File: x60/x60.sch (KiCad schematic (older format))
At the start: 154 parts, among them SW1 SW_Push, U1 ATmega32U4-AU, Y1 16mhz

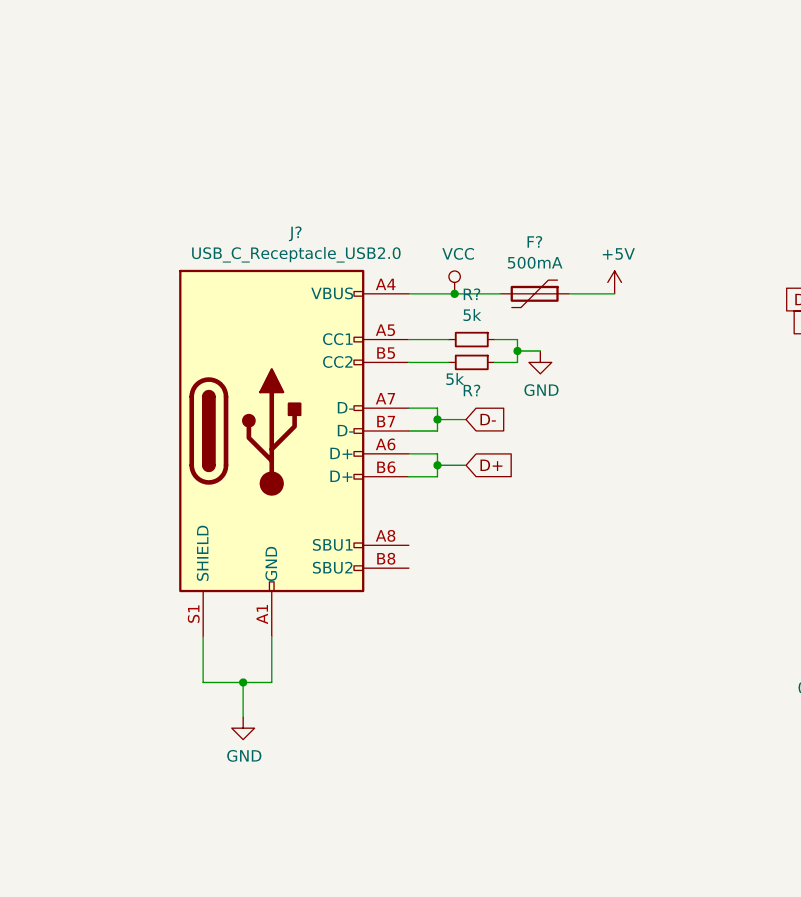
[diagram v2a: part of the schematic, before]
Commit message: redid usbc integration
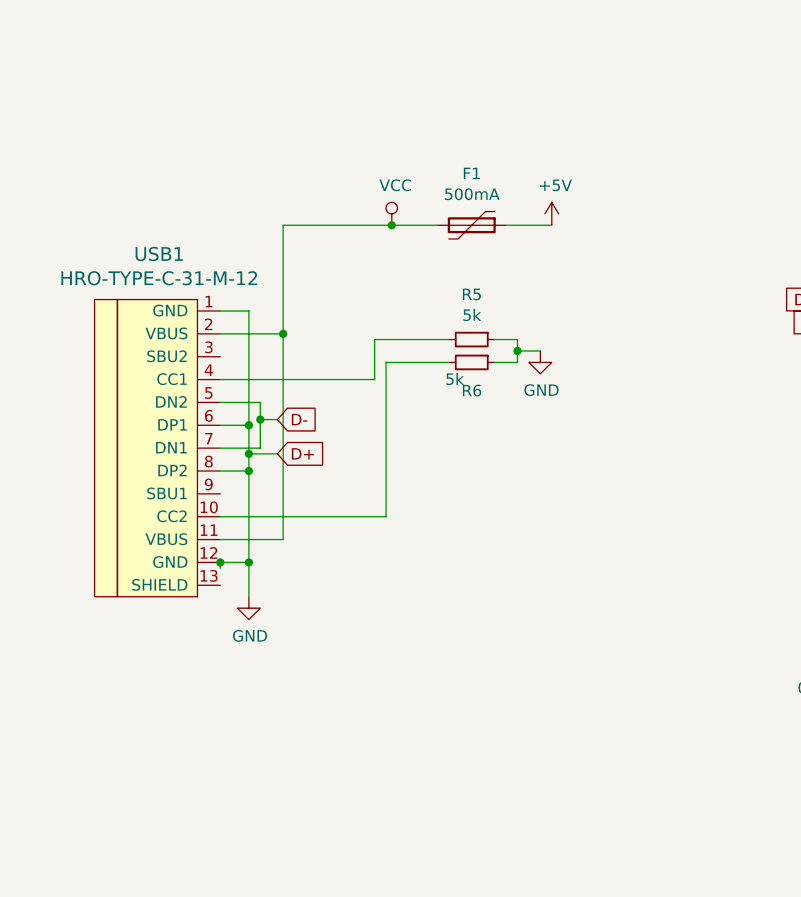
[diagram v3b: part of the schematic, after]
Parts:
- removed J?: USB_C_Receptacle_USB2.0, symbol Connector:USB_C_Receptacle_USB2.0
- added USB1: HRO-TYPE-C-31-M-12, Type-C:HRO-TYPE-C-31-M-12, symbol Type-C:HRO-TYPE-C-31-M-12
- F1: renamed from F?; footprint (none) -> Fuse:Fuse_1206_3216Metric
- R5, R6: renamed from R?; footprint (none) -> Resistor_SMD:R_0805_2012Metric
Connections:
- net D+ is gone; now on net GND: R2.2
- net D-: now also USB1.5 (DN2), USB1.7 (DN1)
- net GND: now also USB1.1 (GND), USB1.12 (GND), USB1.6 (DP1), USB1.8 (DP2)
- net VCC: now also USB1.11 (VBUS), USB1.2 (VBUS)
- net at R5.2: now also USB1.4 (CC1)
- net at R6.2: now also USB1.10 (CC2)
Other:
- moved on the sheet: F1
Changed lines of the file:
@@
 COL14
 $Comp
-L Connector:USB_C_Receptacle_USB2.0 J?
-U 1 1 61856F2E
-P 1575 6850
-F 0 "J?" H 1682 7717 50  0000 C CNN
-F 1 "USB_C_Receptacle_USB2.0" H 1682 7626 50  0000 C CNN
-F 2 "" H 1725 6850 50  0001 C CNN
-F 3 "https://www.usb.org/sites/default/files/documents/usb_type-c.zip" H 1725 6850 50  0001 C CNN
-	1    1575 6850
+L power:GND #PWR0101
+U 1 1 618A0C63
+P 1475 7575
+F 0 "#PWR0101" H 1475 7325 50  0001 C CNN
+F 1 "GND" H 1480 7402 50  0000 C CNN
+F 2 "" H 1475 7575 50  0001 C CNN
+F 3 "" H 1475 7575 50  0001 C CNN
+	1    1475 7575
 	1    0    0    -1
 $EndComp
-Wire Wire Line
-	1275 7750 1275 7950
-Wire Wire Line
-	1275 7950 1450 7950
-Wire Wire Line
-	1575 7950 1575 7750
-Wire Wire Line
-	1450 7950 1450 8100
-Connection ~ 1450 7950
-Wire Wire Line
-	1450 7950 1575 7950
+Text GLabel 1600 6950 2    50   Input ~ 0
+D+
+Text GLabel 1600 6800 2    50   Input ~ 0
+D-
 $Comp
-L power:GND #PWR?
-U 1 1 618A0C63
-P 1450 8100
-F 0 "#PWR?" H 1450 7850 50  0001 C CNN
-F 1 "GND" H 1455 7927 50  0000 C CNN
-F 2 "" H 1450 8100 50  0001 C CNN
-F 3 "" H 1450 8100 50  0001 C CNN
-	1    1450 8100
-	1    0    0    -1
-$EndComp
-Wire Wire Line
-	2175 6950 2300 6950
-Wire Wire Line
-	2300 6950 2300 7000
-Wire Wire Line
-	2300 7050 2175 7050
-Wire Wire Line
-	2300 7000 2425 7000
-Connection ~ 2300 7000
-Wire Wire Line
-	2300 7000 2300 7050
-Text GLabel 2425 7000 2    50   Input ~ 0
-D+
-Wire Wire Line
-	2175 6750 2300 6750
-Wire Wire Line
-	2300 6750 2300 6800
-Wire Wire Line
-	2300 6850 2175 6850
-Wire Wire Line
-	2300 6800 2425 6800
-Connection ~ 2300 6800
-Wire Wire Line
-	2300 6800 2300 6850
-Text GLabel 2425 6800 2    50   Input ~ 0
-D-
-Wire Wire Line
-	2175 6450 2350 6450
-Wire Wire Line
-	2175 6550 2350 6550
-$Comp
-L Device:R_Small R?
+L Device:R_Small R5
 U 1 1 6198B265
 P 2450 6450
-F 0 "R?" V 2254 6450 50  0000 C CNN
+F 0 "R5" V 2254 6450 50  0000 C CNN
 F 1 "5k" V 2345 6450 50  0000 C CNN
-F 2 "" H 2450 6450 50  0001 C CNN
+F 2 "Resistor_SMD:R_0805_2012Metric" H 2450 6450 50  0001 C CNN
 F 3 "~" H 2450 6450 50  0001 C CNN
 	1    2450 6450
@@
 $EndComp
 $Comp
-L Device:R_Small R?
+L Device:R_Small R6
 U 1 1 6198B998
 P 2450 6550
-F 0 "R?" V 2575 6550 50  0000 C CNN
+F 0 "R6" V 2575 6550 50  0000 C CNN
 F 1 "5k" V 2525 6475 50  0000 C CNN
-F 2 "" H 2450 6550 50  0001 C CNN
+F 2 "Resistor_SMD:R_0805_2012Metric" H 2450 6550 50  0001 C CNN
 F 3 "~" H 2450 6550 50  0001 C CNN
 	1    2450 6550
@@
 	2650 6500 2650 6450
 $Comp
-L power:GND #PWR?
+L power:GND #PWR0102
 U 1 1 61A598C2
 P 2750 6500
-F 0 "#PWR?" H 2750 6250 50  0001 C CNN
+F 0 "#PWR0102" H 2750 6250 50  0001 C CNN
 F 1 "GND" H 2755 6327 50  0000 C CNN
 F 2 "" H 2750 6500 50  0001 C CNN
@@
 	1    0    0    -1
 $EndComp
-Wire Wire Line
-	2175 6250 2375 6250
 $Comp
-L power:VCC #PWR?
+L power:VCC #PWR0103
 U 1 1 61A8443F
-P 2375 6250
-F 0 "#PWR?" H 2375 6100 50  0001 C CNN
-F 1 "VCC" H 2392 6423 50  0000 C CNN
-F 2 "" H 2375 6250 50  0001 C CNN
-F 3 "" H 2375 6250 50  0001 C CNN
-	1    2375 6250
+P 2100 5950
+F 0 "#PWR0103" H 2100 5800 50  0001 C CNN
+F 1 "VCC" H 2117 6123 50  0000 C CNN
+F 2 "" H 2100 5950 50  0001 C CNN
+F 3 "" H 2100 5950 50  0001 C CNN
+	1    2100 5950
 	1    0    0    -1
 $EndComp
 Wire Wire Line
-	2375 6250 2575 6250
-Connection ~ 2375 6250
+	2100 5950 2300 5950
+Connection ~ 2100 5950
 $Comp
-L Device:Polyfuse F?
+L Device:Polyfuse F1
 U 1 1 61AAEE5C
-P 2725 6250
-F 0 "F?" V 2500 6250 50  0000 C CNN
-F 1 "500mA" V 2591 6250 50  0000 C CNN
-F 2 "" H 2775 6050 50  0001 L CNN
-F 3 "~" H 2725 6250 50  0001 C CNN
-	1    2725 6250
+P 2450 5950
+F 0 "F1" V 2225 5950 50  0000 C CNN
+F 1 "500mA" V 2316 5950 50  0000 C CNN
+F 2 "Fuse:Fuse_1206_3216Metric" H 2500 5750 50  0001 L CNN
+F 3 "~" H 2450 5950 50  0001 C CNN
+	1    2450 5950
 	0    1    1    0
 $EndComp
 Wire Wire Line
-	2875 6250 3075 6250
+	2600 5950 2800 5950
 $Comp
-L power:+5V #PWR?
+L power:+5V #PWR0104
 U 1 1 61ADB3C8
-P 3075 6250
-F 0 "#PWR?" H 3075 6100 50  0001 C CNN
-F 1 "+5V" H 3090 6423 50  0000 C CNN
-F 2 "" H 3075 6250 50  0001 C CNN
-F 3 "" H 3075 6250 50  0001 C CNN
-	1    3075 6250
+P 2800 5950
+F 0 "#PWR0104" H 2800 5800 50  0001 C CNN
+F 1 "+5V" H 2815 6123 50  0000 C CNN
+F 2 "" H 2800 5950 50  0001 C CNN
+F 3 "" H 2800 5950 50  0001 C CNN
+	1    2800 5950
 	1    0    0    -1
 $EndComp
+$Comp
+L Type-C:HRO-TYPE-C-31-M-12 USB1
+U 1 1 6184BA5C
+P 1250 6875
+F 0 "USB1" H 1083 7672 60  0000 C CNN
+F 1 "HRO-TYPE-C-31-M-12" H 1083 7566 60  0000 C CNN
+F 2 "Type-C:HRO-TYPE-C-31-M-12" H 1250 6875 60  0001 C CNN
+F 3 "" H 1250 6875 60  0001 C CNN
+	1    1250 6875
+	1    0    0    -1
+$EndComp
+Wire Wire Line
+	1350 6625 2025 6625
+Wire Wire Line
+	2025 6625 2025 6450
+Wire Wire Line
+	2025 6450 2350 6450
+Wire Wire Line
+	1350 7225 2075 7225
+Wire Wire Line
+	2075 7225 2075 6550
+Wire Wire Line
+	2075 6550 2350 6550
+Wire Wire Line
+	1350 6925 1525 6925
+Wire Wire Line
+	1525 6925 1525 6800
+Wire Wire Line
+	1525 6725 1350 6725
+Wire Wire Line
+	1525 6800 1600 6800
+Connection ~ 1525 6800
+Wire Wire Line
+	1525 6800 1525 6725
+Wire Wire Line
+	1350 6825 1475 6825
+Wire Wire Line
+	1475 6825 1475 6950
+Wire Wire Line
+	1475 7025 1350 7025
+Wire Wire Line
+	1475 6950 1600 6950
+Connection ~ 1475 6950
+Wire Wire Line
+	1475 6950 1475 7025
+Wire Wire Line
+	1350 6425 1625 6425
+Wire Wire Line
+	1625 6425 1625 7325
+Wire Wire Line
+	1625 7325 1350 7325
+Wire Wire Line
+	1625 6425 1625 5950
+Wire Wire Line
+	1625 5950 2100 5950
+Connection ~ 1625 6425
+Wire Wire Line
+	1350 6325 1475 6325
+Wire Wire Line
+	1475 6325 1475 6825
+Connection ~ 1475 6825
+Connection ~ 1475 7025
+Wire Wire Line
+	1475 7025 1475 7425
+Wire Wire Line
+	1350 7450 1350 7425
+Wire Wire Line
+	1350 7425 1475 7425
+Connection ~ 1350 7425
+Wire Wire Line
+	1475 7425 1475 7575
+Connection ~ 1475 7425
 $EndSCHEMATC

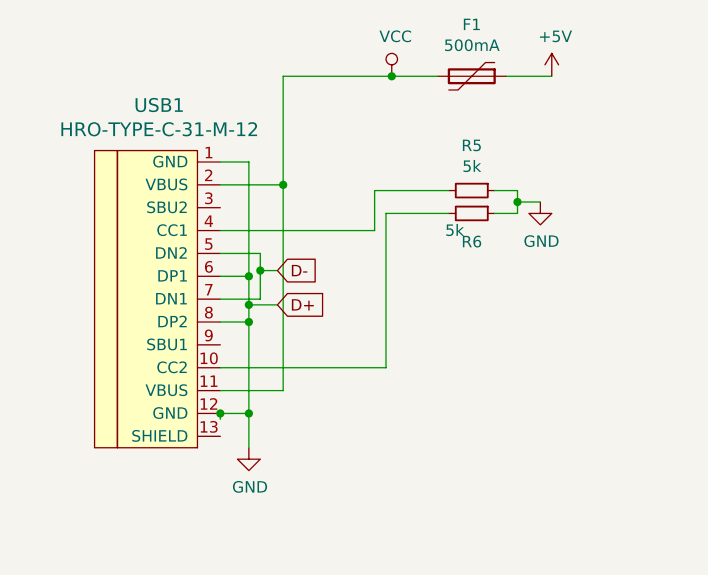
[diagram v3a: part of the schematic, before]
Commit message: wired usb port
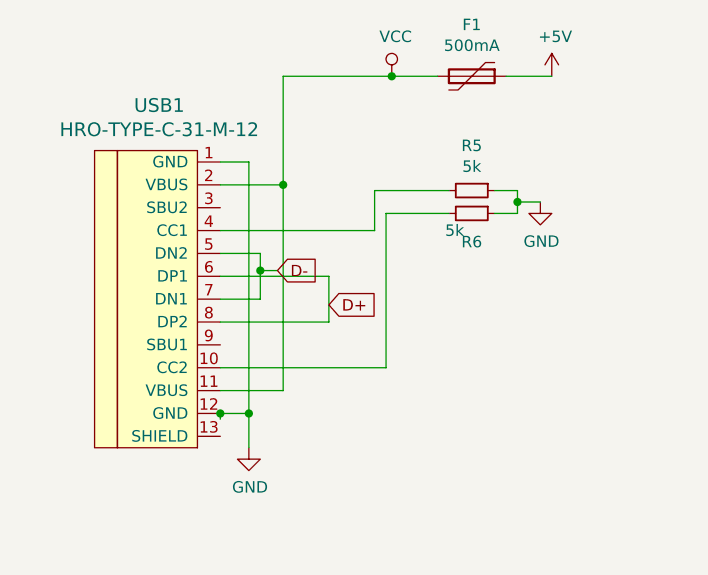
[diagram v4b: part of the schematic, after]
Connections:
- net GND: no longer R2.2, USB1.6 (DP1), USB1.8 (DP2)
- new net D+: R2.2, USB1.6 (DP1), USB1.8 (DP2)
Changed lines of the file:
@@
 	1    0    0    -1
 $EndComp
-Text GLabel 1600 6950 2    50   Input ~ 0
+Text GLabel 1825 6950 2    50   Input ~ 0
 D+
 Text GLabel 1600 6800 2    50   Input ~ 0
@@
 	1525 6800 1525 6725
 Wire Wire Line
-	1350 6825 1475 6825
-Wire Wire Line
-	1475 6825 1475 6950
-Wire Wire Line
-	1475 7025 1350 7025
-Wire Wire Line
-	1475 6950 1600 6950
-Connection ~ 1475 6950
-Wire Wire Line
-	1475 6950 1475 7025
-Wire Wire Line
 	1350 6425 1625 6425
 Wire Wire Line
@@
 	1350 6325 1475 6325
 Wire Wire Line
-	1475 6325 1475 6825
-Connection ~ 1475 6825
-Connection ~ 1475 7025
-Wire Wire Line
-	1475 7025 1475 7425
-Wire Wire Line
 	1350 7450 1350 7425
 Wire Wire Line
@@
 	1475 7425 1475 7575
 Connection ~ 1475 7425
+Wire Wire Line
+	1475 6325 1475 7425
+Wire Wire Line
+	1350 6825 1825 6825
+Wire Wire Line
+	1350 7025 1825 7025
+Wire Wire Line
+	1825 6825 1825 7025
 $EndSCHEMATC
